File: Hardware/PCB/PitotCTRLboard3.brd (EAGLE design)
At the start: 17.8 x 75.1 mm, 67 parts, among them J1 2201778-1, U1 STM32F405RGT6, U2 MAX1595EUA33+

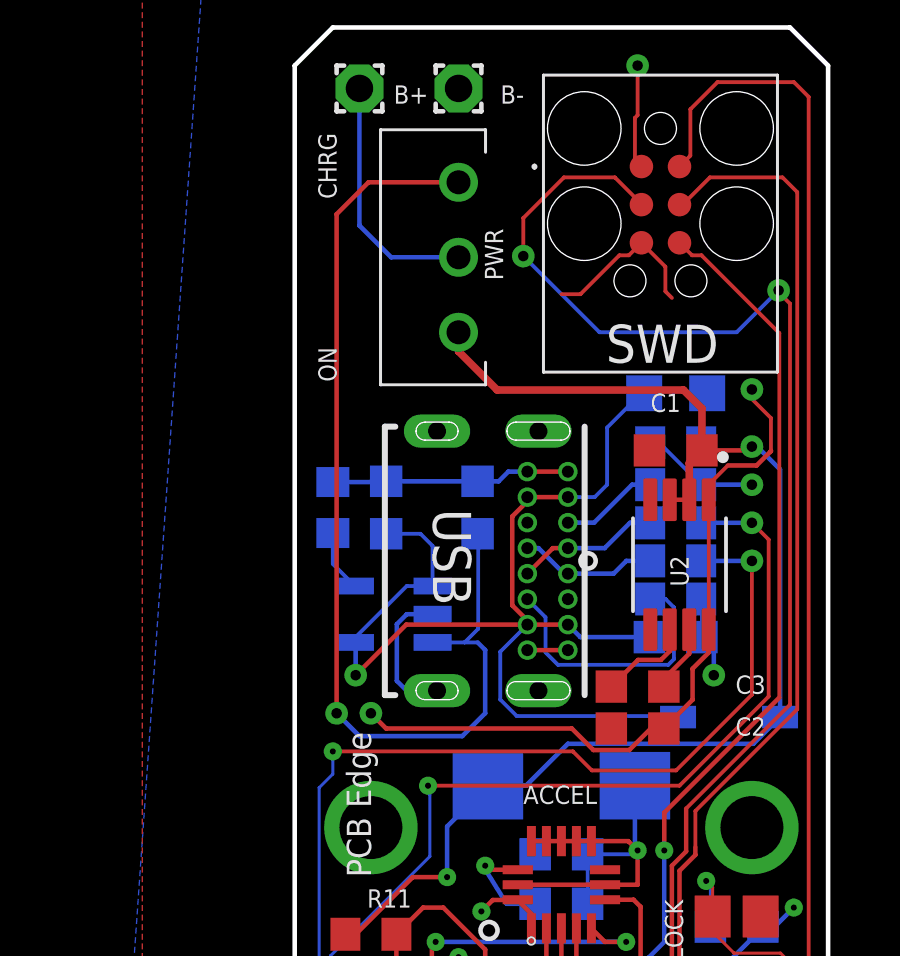
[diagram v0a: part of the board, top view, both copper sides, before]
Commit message: fix a via under usb-c
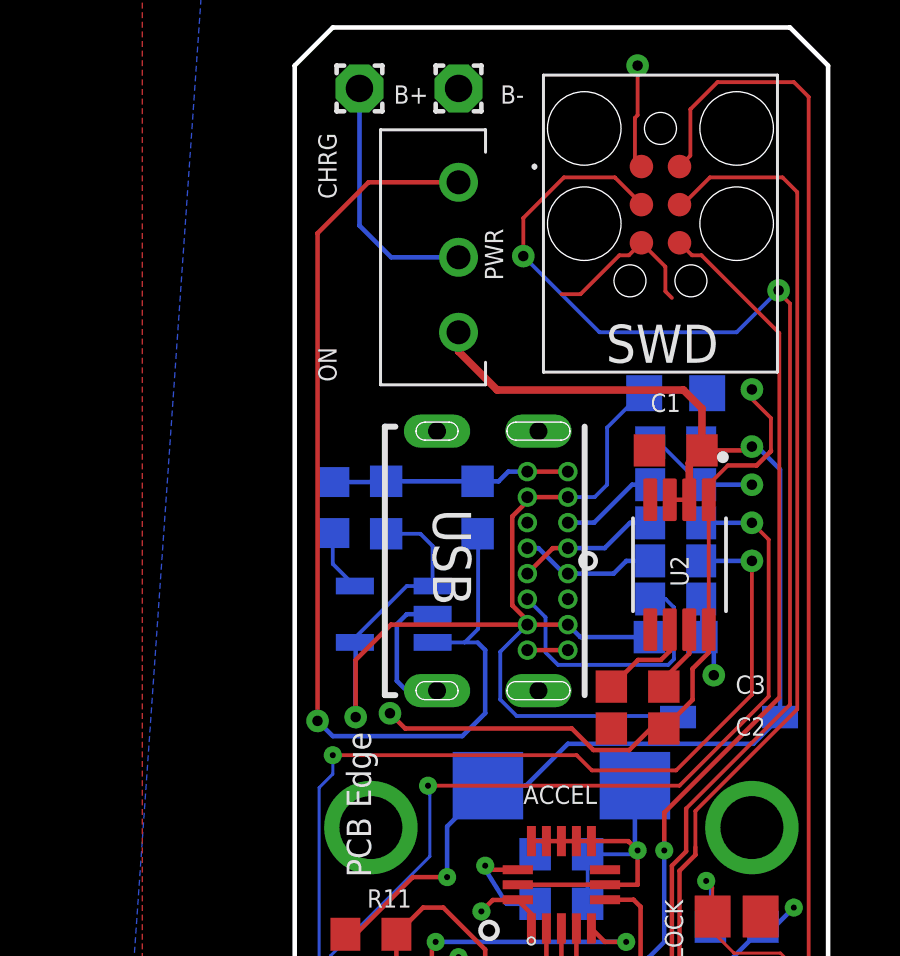
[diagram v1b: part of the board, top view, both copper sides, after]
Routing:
- net +5V: track 38.5 -> 41.6 mm
- net N$38: track 34.6 -> 35.7 mm
- net +3V3: track 82.2 -> 81.5 mm
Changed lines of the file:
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@@
 <wire x1="5.547" y1="24.771" x2="4.912" y2="24.136" width="0.127" layer="1"/>
 <wire x1="6.985" y1="25.273" x2="6.985" y2="26.35065625" width="0.127" layer="1"/>
-<wire x1="-5.842" y1="16.002" x2="-6.35" y2="16.51" width="0.1524" layer="1"/>
+<wire x1="-5.207" y1="16.002" x2="-5.715" y2="16.51" width="0.1524" layer="1"/>
 <wire x1="2.26365" y1="15.2842" x2="1.06635" y2="15.2842" width="0.1524" layer="1"/>
 <wire x1="3.415" y1="16.002" x2="2.98145" y2="16.002" width="0.1524" layer="1"/>
-<wire x1="0.34855" y1="16.002" x2="-5.842" y2="16.002" width="0.1524" layer="1"/>
+<wire x1="0.34855" y1="16.002" x2="-5.207" y2="16.002" width="0.1524" layer="1"/>
 <wire x1="2.98145" y1="16.002" x2="2.26365" y2="15.2842" width="0.1524" layer="1"/>
 <wire x1="1.06635" y1="15.2842" x2="0.34855" y2="16.002" width="0.1524" layer="1"/>
-<via x="-6.35" y="16.51" extent="1-16" drill="0.35"/>
+<via x="-5.715" y="16.51" extent="1-16" drill="0.35"/>
 <wire x1="5.547" y1="24.771" x2="6.50730625" y2="24.771" width="0.1524" layer="1"/>
 <wire x1="6.985" y1="25.24869375" x2="6.985" y2="25.273" width="0.1524" layer="1"/>
@@
 <wire x1="-2.0381" y1="18.5619" x2="-1.135" y2="19.465" width="0.127" layer="16"/>
 <wire x1="-6.8834" y1="18.8722" x2="-6.858" y2="18.8468" width="0.1524" layer="16"/>
-<wire x1="-6.858" y1="18.8468" x2="-6.858" y2="17.78" width="0.1524" layer="16"/>
-<via x="-6.858" y="17.78" extent="1-16" drill="0.35"/>
-<wire x1="-6.858" y1="17.78" x2="-5.173" y2="19.465" width="0.1524" layer="1"/>
-<wire x1="-5.173" y1="19.465" x2="-1.135" y2="19.465" width="0.1524" layer="1"/>
+<wire x1="-6.858" y1="18.8468" x2="-6.858" y2="16.383" width="0.1524" layer="16"/>
+<via x="-6.858" y="16.383" extent="1-16" drill="0.35"/>
+<wire x1="-6.858" y1="16.383" x2="-6.858" y2="18.288" width="0.1524" layer="1"/>
+<wire x1="-5.681" y1="19.465" x2="-6.858" y2="18.288" width="0.1524" layer="1"/>
+<wire x1="-5.681" y1="19.465" x2="-1.135" y2="19.465" width="0.1524" layer="1"/>
 </signal>
 <signal name="V+">
@@
 <wire x1="-2.7747125" y1="19.3232875" x2="-2.7747125" y2="22.493" width="0.127" layer="16"/>
 <wire x1="-3.2258" y1="18.8722" x2="-2.7747125" y2="19.3232875" width="0.127" layer="16"/>
-<wire x1="-7.479" y1="16.524" x2="-7.493" y2="16.51" width="0.1524" layer="16"/>
-<via x="-7.493" y="16.51" extent="1-16" drill="0.35"/>
-<wire x1="-7.493" y1="16.51" x2="-7.493" y2="33.147" width="0.1524" layer="1"/>
-<wire x1="-6.43" y1="34.21" x2="-7.493" y2="33.147" width="0.1524" layer="1"/>
+<wire x1="-8.114" y1="16.27" x2="-8.128" y2="16.256" width="0.1524" layer="16"/>
+<via x="-8.128" y="16.256" extent="1-16" drill="0.35"/>
+<wire x1="-8.128" y1="16.256" x2="-8.128" y2="32.512" width="0.1524" layer="1"/>
+<wire x1="-6.43" y1="34.21" x2="-8.128" y2="32.512" width="0.1524" layer="1"/>
 <wire x1="-6.43" y1="34.21" x2="-3.429" y2="34.21" width="0.1524" layer="1"/>
-<wire x1="-7.493" y1="16.51" x2="-6.731" y2="15.748" width="0.1524" layer="16"/>
-<wire x1="-6.731" y1="15.748" x2="-3.302" y2="15.748" width="0.1524" layer="16"/>
+<wire x1="-8.128" y1="16.256" x2="-7.62" y2="15.748" width="0.1524" layer="16"/>
+<wire x1="-7.62" y1="15.748" x2="-3.302" y2="15.748" width="0.1524" layer="16"/>
 <wire x1="-3.302" y1="15.748" x2="-2.54" y2="16.51" width="0.1524" layer="16"/>
 <wire x1="-2.54" y1="16.51" x2="-2.54" y2="18.6182" width="0.1524" layer="16"/>
@@
 <wire x1="-7.366" y1="-3.4769125" x2="-7.366" y2="-3.556" width="0.1016" layer="1"/>
 <via x="-7.366" y="-3.556" extent="1-16" drill="0.2"/>
-<wire x1="-7.62" y1="14.483875" x2="-7.62" y2="15.24" width="0.1016" layer="16"/>
+<wire x1="-7.62" y1="14.483875" x2="-7.62" y2="15.113" width="0.1016" layer="16"/>
 <wire x1="-8.0756" y1="-1.7034" x2="-8.0756" y2="14.028275" width="0.1016" layer="16"/>
 <wire x1="-8.0756" y1="14.028275" x2="-7.62" y2="14.483875" width="0.1016" layer="16"/>
 <wire x1="-7.366" y1="-3.556" x2="-7.366" y2="-2.413" width="0.1016" layer="16"/>
 <wire x1="-7.366" y1="-2.413" x2="-8.0756" y2="-1.7034" width="0.1016" layer="16"/>
-<via x="-7.62" y="15.24" extent="1-16" drill="0.2"/>
+<via x="-7.62" y="15.113" extent="1-16" drill="0.2"/>
 <wire x1="4.66" y1="21.59" x2="6.35" y2="21.59" width="0.1524" layer="16"/>
 <via x="6.35" y="21.59" extent="1-16" drill="0.35"/>
 <wire x1="3.8244875" y1="14.605" x2="6.35" y2="17.1305125" width="0.127" layer="1"/>
 <wire x1="6.35" y1="17.1305125" x2="6.35" y2="21.59" width="0.127" layer="1"/>
-<wire x1="-7.62" y1="15.24" x2="0.381" y2="15.24" width="0.127" layer="1"/>
-<wire x1="1.016" y1="14.605" x2="0.381" y2="15.24" width="0.127" layer="1"/>
+<wire x1="-7.62" y1="15.113" x2="0.508" y2="15.113" width="0.127" layer="1"/>
+<wire x1="1.016" y1="14.605" x2="0.508" y2="15.113" width="0.127" layer="1"/>
 <wire x1="3.8244875" y1="14.605" x2="1.016" y2="14.605" width="0.127" layer="1"/>
 </signal>
